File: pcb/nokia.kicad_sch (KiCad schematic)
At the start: 96 parts, among them J1 Conn_01x07, J2 USB_B_Micro, J20 Conn_01x04_Pin, J3 SM03B-SRSS-TB, J4 Conn_01x06_Pin, J5 Conn_02x10_Top_Bottom, J6 SM03B-SRSS-TB, M1 Vibration, Q1 BC847, SW1 SW_Push, U1 W25Q128JVS, U4 NCP1117-3.3_SOT223, U5 RP2350_80QFN, Y1 ABM8-272-T3

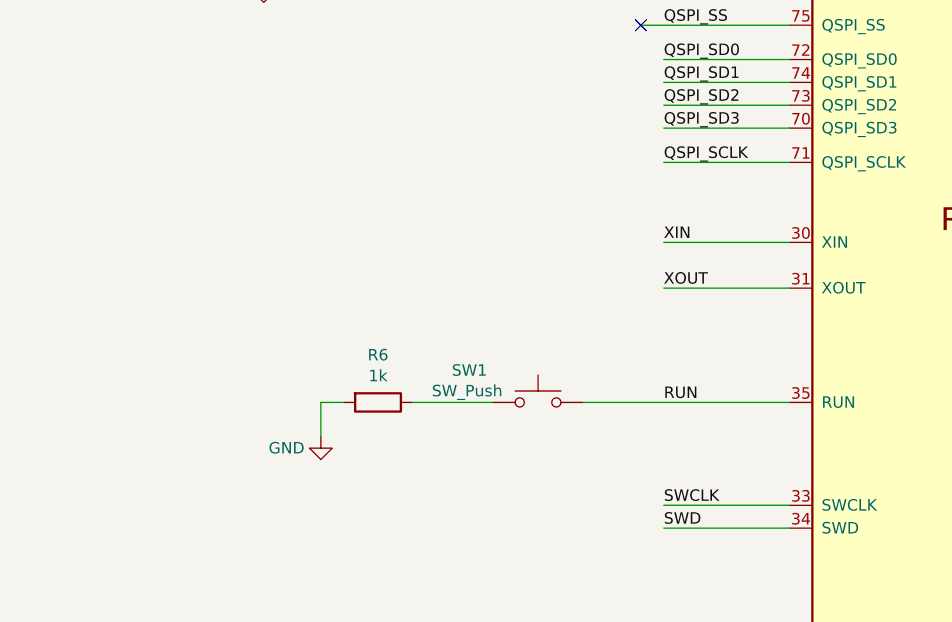
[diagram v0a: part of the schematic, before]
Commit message: power button can be gpio or run
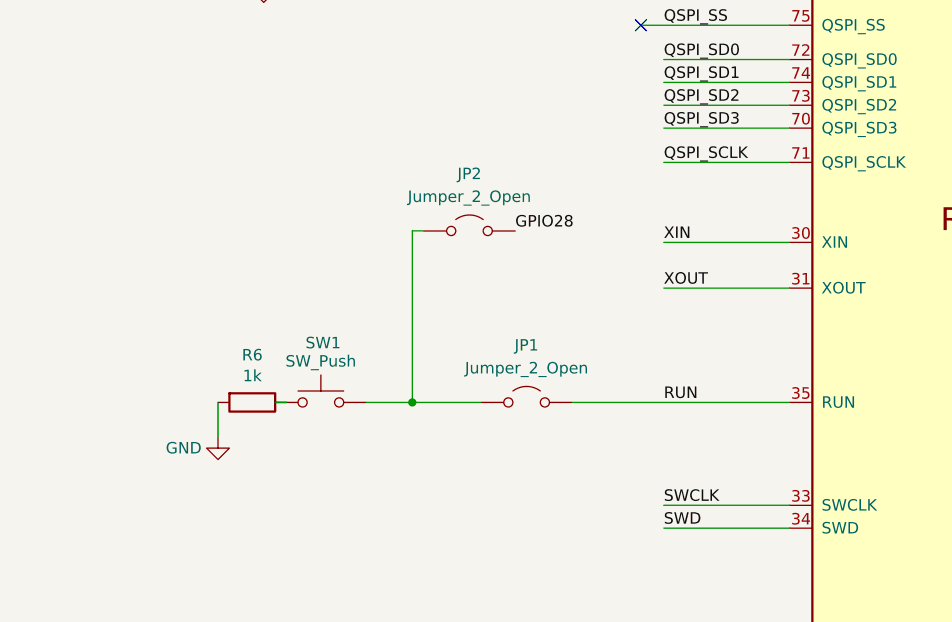
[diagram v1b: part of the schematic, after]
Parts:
- added JP1, JP2: Jumper_2_Open, Jumper:SolderJumper-2_P1.3mm_Open_RoundedPad1.0x1.5mm, symbol Jumper:Jumper_2_Open
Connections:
- net GPIO28: now also JP2.2 (B)
- net RUN: now also JP1.2 (B); no longer SW1.2
- new net: JP1.1 (A), JP2.1 (A), SW1.2
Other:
- moved on the sheet: R6, SW1
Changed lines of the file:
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@@
 	)
 	(junction
+		(at 200.66 129.54)
+		(diameter 0)
+		(color 0 0 0 0)
+	)
+	(junction
 		(at 373.38 36.83)
 		(diameter 0)
@@
 	(wire
 		(pts
+			(xy 200.66 129.54) (xy 208.28 129.54)
+		)
+		(stroke
+			(width 0)
+			(type default)
+		)
+	)
+	(wire
+		(pts
 			(xy 311.15 111.76) (xy 326.39 111.76)
 		)
@@
 	(wire
 		(pts
+			(xy 201.93 110.49) (xy 200.66 110.49)
+		)
+		(stroke
+			(width 0)
+			(type default)
+		)
+	)
+	(wire
+		(pts
 			(xy 90.17 212.09) (xy 90.17 208.28)
 		)
@@
 	(wire
 		(pts
+			(xy 218.44 129.54) (xy 242.57 129.54)
+		)
+		(stroke
+			(width 0)
+			(type default)
+		)
+	)
+	(wire
+		(pts
 			(xy 177.8 264.16) (xy 175.26 264.16)
 		)
@@
 	(wire
 		(pts
-			(xy 200.66 129.54) (xy 209.55 129.54)
+			(xy 186.69 129.54) (xy 185.42 129.54)
 		)
 		(stroke
@@
 	(wire
 		(pts
+			(xy 195.58 129.54) (xy 200.66 129.54)
+		)
+		(stroke
+			(width 0)
+			(type default)
+		)
+	)
+	(wire
+		(pts
 			(xy 127 259.08) (xy 127 257.81)
 		)
@@
 	(wire
 		(pts
-			(xy 219.71 129.54) (xy 242.57 129.54)
-		)
-		(stroke
-			(width 0)
-			(type default)
-		)
-	)
-	(wire
-		(pts
 			(xy 327.66 36.83) (xy 316.23 36.83)
 		)
@@
 	(wire
 		(pts
+			(xy 200.66 110.49) (xy 200.66 129.54)
+		)
+		(stroke
+			(width 0)
+			(type default)
+		)
+	)
+	(wire
+		(pts
 			(xy 264.16 45.72) (xy 270.51 45.72)
 		)
@@
 	(wire
 		(pts
-			(xy 190.5 129.54) (xy 190.5 133.35)
+			(xy 179.07 129.54) (xy 179.07 133.35)
 		)
 		(stroke
@@
 	(wire
 		(pts
-			(xy 193.04 129.54) (xy 190.5 129.54)
-		)
-		(stroke
-			(width 0)
-			(type default)
-		)
-	)
-	(wire
-		(pts
 			(xy 270.51 233.68) (xy 268.605 233.68)
 		)
@@
 		)
 	)
+	(label "GPIO28"
+		(at 212.09 110.49 0)
+		(fields_autoplaced yes)
+		(effects
+			(font
+				(size 1.27 1.27)
+			)
+			(justify left bottom)
+		)
+	)
 	(label "GPIO32"
 		(at 29.21 124.46 0)
@@
 	)
 	(symbol
+		(lib_id "Jumper:Jumper_2_Open")
+		(at 213.36 129.54 0)
+		(unit 1)
+		(exclude_from_sim yes)
+		(in_bom yes)
+		(on_board yes)
+		(dnp no)
+		(fields_autoplaced yes)
+		(property "Reference" "JP1"
+			(at 213.36 123.19 0)
+			(effects
+				(font
+					(size 1.27 1.27)
+				)
+			)
+		)
+		(property "Value" "Jumper_2_Open"
+			(at 213.36 125.73 0)
+			(effects
+				(font
+					(size 1.27 1.27)
+				)
+			)
+		)
+		(property "Footprint" "Jumper:SolderJumper-2_P1.3mm_Open_RoundedPad1.0x1.5mm"
+			(at 213.36 129.54 0)
+			(effects
+				(font
+					(size 1.27 1.27)
+				)
+				(hide yes)
+			)
+		)
+		(property "Datasheet" "~"
+			(at 213.36 129.54 0)
+			(effects
+				(font
+					(size 1.27 1.27)
+				)
+				(hide yes)
+			)
+		)
+		(property "Description" "Jumper, 2-pole, open"
+			(at 213.36 129.54 0)
+			(effects
+				(font
+					(size 1.27 1.27)
+				)
+				(hide yes)
+			)
+		)
+		(pin "1"
+		)
+		(pin "2"
+		)
+		(instances
+			(project ""
+				(path "/3906e17f-1a23-46f4-8c63-f34176cde9d9"
+					(reference "JP1")
+					(unit 1)
+				)
+			)
+		)
+	)
+	(symbol
 		(lib_name "LED_ARGB_1")
 		(lib_id "Device:LED_ARGB")
@@
 	(symbol
 		(lib_id "Device:R")
-		(at 196.85 129.54 270)
+		(at 182.88 129.54 270)
 		(unit 1)
 		(exclude_from_sim no)
@@
 		(dnp no)
 		(property "Reference" "R6"
-			(at 196.85 124.2822 90)
+			(at 182.88 124.2822 90)
 			(effects
 				(font
@@
 		)
 		(property "Value" "1k"
-			(at 196.85 126.5936 90)
+			(at 182.88 126.5936 90)
 			(effects
 				(font
@@
 		)
 		(property "Footprint" "Resistor_SMD:R_0402_1005Metric"
-			(at 196.85 127.762 90)
+			(at 182.88 127.762 90)
 			(effects
 				(font
@@
 		)
 		(property "Datasheet" "~"
-			(at 196.85 129.54 0)
+			(at 182.88 129.54 0)
 			(effects
 				(font
@@
 		)
 		(property "Description" ""
-			(at 196.85 129.54 0)
+			(at 182.88 129.54 0)
 			(effects
 				(font
@@
 	)
 	(symbol
+		(lib_id "Jumper:Jumper_2_Open")
+		(at 207.01 110.49 0)
+		(unit 1)
+		(exclude_from_sim yes)
+		(in_bom yes)
+		(on_board yes)
+		(dnp no)
+		(fields_autoplaced yes)
+		(property "Reference" "JP2"
+			(at 207.01 104.14 0)
+			(effects
+				(font
+					(size 1.27 1.27)
+				)
+			)
+		)
+		(property "Value" "Jumper_2_Open"
+			(at 207.01 106.68 0)
+			(effects
+				(font
+					(size 1.27 1.27)
+				)
+			)
+		)
+		(property "Footprint" "Jumper:SolderJumper-2_P1.3mm_Open_RoundedPad1.0x1.5mm"
+			(at 207.01 110.49 0)
+			(effects
+				(font
+					(size 1.27 1.27)
+				)
+				(hide yes)
+			)
+		)
+		(property "Datasheet" "~"
+			(at 207.01 110.49 0)
+			(effects
+				(font
+					(size 1.27 1.27)
+				)
+				(hide yes)
+			)
+		)
+		(property "Description" "Jumper, 2-pole, open"
+			(at 207.01 110.49 0)
+			(effects
+				(font
+					(size 1.27 1.27)
+				)
+				(hide yes)
+			)
+		)
+		(pin "1"
+		)
+		(pin "2"
+		)
+		(instances
+			(project "nokia"
+				(path "/3906e17f-1a23-46f4-8c63-f34176cde9d9"
+					(reference "JP2")
+					(unit 1)
+				)
+			)
+		)
+	)
+	(symbol
 		(lib_id "Device:R")
 		(at 64.77 116.84 180)
@@
 	(symbol
 		(lib_id "power:GND")
-		(at 190.5 133.35 0)
+		(at 179.07 133.35 0)
 		(unit 1)
 		(exclude_from_sim no)
@@
 		(dnp no)
 		(property "Reference" "#PWR024"
-			(at 190.5 139.7 0)
+			(at 179.07 139.7 0)
 			(effects
 				(font
@@
 		)
 		(property "Value" "GND"
-			(at 186.69 134.62 0)
+			(at 175.26 134.62 0)
 			(effects
 				(font
@@
 		)
 		(property "Footprint" ""
-			(at 190.5 133.35 0)
+			(at 179.07 133.35 0)
 			(effects
 				(font
@@
 		)
 		(property "Datasheet" ""
-			(at 190.5 133.35 0)
+			(at 179.07 133.35 0)
 			(effects
 				(font
@@
 		)
 		(property "Description" ""
-			(at 190.5 133.35 0)
+			(at 179.07 133.35 0)
 			(effects
 				(font
@@
 	(symbol
 		(lib_id "Switch:SW_Push")
-		(at 214.63 129.54 0)
+		(at 190.5 129.54 0)
 		(unit 1)
 		(exclude_from_sim no)
@@
 		(dnp no)
 		(property "Reference" "SW1"
-			(at 207.01 125.984 0)
+			(at 190.754 122.936 0)
 			(effects
 				(font
@@
 		)
 		(property "Value" "SW_Push"
-			(at 206.756 128.27 0)
+			(at 190.5 124.968 0)
 			(effects
 				(font
@@
 		)
 		(property "Footprint" "Button_Switch_SMD:power switch"
-			(at 214.63 124.46 0)
+			(at 190.5 124.46 0)
 			(effects
 				(font
@@
 		)
 		(property "Datasheet" "~"
-			(at 214.63 124.46 0)
+			(at 190.5 124.46 0)
 			(effects
 				(font
@@
 		)
 		(property "Description" "Push button switch, generic, two pins"
-			(at 214.63 129.54 0)
+			(at 190.5 129.54 0)
 			(effects
 				(font

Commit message: make corrections
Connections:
- net GPIO30: now also R11.1, R14.1, R16.1, R19.1, R22.1, R25.1, R28.1, R31.1; no longer R13.2, R18.2, R21.2, R24.2, R27.2, R30.2, R4.2, R5.2
- net GPIO32: now also R13.2, R18.2, R21.2, R24.2, R27.2, R30.2, R4.2, R5.2; no longer R11.1, R14.1, R16.1, R19.1, R22.1, R25.1, R28.1, R31.1
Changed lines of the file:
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@@
 		)
 	)
-	(label "GPIO32"
+	(label "GPIO30"
 		(at 52.07 210.82 0)
 		(fields_autoplaced yes)
@@
 		)
 	)
-	(label "GPIO30"
+	(label "GPIO32"
 		(at 46.99 213.36 0)
 		(fields_autoplaced yes)
@@
 		)
 	)
-	(label "GPIO30"
+	(label "GPIO32"
 		(at 93.98 175.26 0)
 		(fields_autoplaced yes)
@@
 		)
 	)
-	(label "GPIO30"
+	(label "GPIO32"
 		(at 52.07 127 0)
 		(fields_autoplaced yes)
@@
 		)
 	)
-	(label "GPIO30"
+	(label "GPIO32"
 		(at 90.17 212.09 0)
 		(fields_autoplaced yes)
@@
 		)
 	)
-	(label "GPIO30"
+	(label "GPIO32"
 		(at 46.99 172.72 0)
 		(fields_autoplaced yes)
@@
 		)
 	)
+	(label "GPIO32"
+		(at 106.68 127 0)
+		(fields_autoplaced yes)
+		(effects
+			(font
+				(size 1.27 1.27)
+			)
+			(justify left bottom)
+		)
+	)
 	(label "GPIO30"
-		(at 106.68 127 0)
-		(fields_autoplaced yes)
-		(effects
-			(font
-				(size 1.27 1.27)
-			)
-			(justify left bottom)
-		)
-	)
-	(label "GPIO32"
 		(at 95.25 209.55 0)
 		(fields_autoplaced yes)
@@
 		)
 	)
-	(label "GPIO32"
+	(label "GPIO30"
 		(at 85.09 124.46 0)
 		(fields_autoplaced yes)
@@
 		)
 	)
-	(label "GPIO32"
+	(label "GPIO30"
 		(at 29.21 124.46 0)
 		(fields_autoplaced yes)
@@
 		)
 	)
+	(label "GPIO30"
+		(at 52.07 170.18 0)
+		(fields_autoplaced yes)
+		(effects
+			(font
+				(size 1.27 1.27)
+			)
+			(justify left bottom)
+		)
+	)
 	(label "GPIO32"
-		(at 52.07 170.18 0)
-		(fields_autoplaced yes)
-		(effects
-			(font
-				(size 1.27 1.27)
-			)
-			(justify left bottom)
-		)
-	)
-	(label "GPIO30"
 		(at 24.13 127 0)
 		(fields_autoplaced yes)
@@
 		)
 	)
-	(label "GPIO32"
+	(label "GPIO30"
 		(at 111.76 124.46 0)
 		(fields_autoplaced yes)
@@
 		)
 	)
-	(label "GPIO32"
+	(label "GPIO30"
 		(at 99.06 172.72 0)
 		(fields_autoplaced yes)
@@
 		)
 	)
-	(label "GPIO32"
+	(label "GPIO30"
 		(at 57.15 124.46 0)
 		(fields_autoplaced yes)
@@
 		)
 	)
-	(label "GPIO30"
+	(label "GPIO32"
 		(at 80.01 127 0)
 		(fields_autoplaced yes)

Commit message: fix clearance for screws, more space for connectors, move LEDs
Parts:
- added C22, C24: 100n, Capacitor_SMD:C_0402_1005Metric, symbol Device:C
- added C23: 100m, 5V5, CoreElectronics_Components:Kemet_FC_10.5X5.5, symbol PiicoDev-Real-Time-Clock-RV3028-rescue:CP1-Device
- added JP4: I2C PU, CoreElectronics_Components:SolderJumper-3_P1.3mm_Closed_RoundedPad1.0x1.5mm_NumberLabels, symbol PiicoDev-Real-Time-Clock-RV3028-rescue:SolderJumper_3_Bridged123-Jumper
- added R34, R35, R36, R38: 10k, Resistor_SMD:R_0402_1005Metric, symbol Device:R
- added R37: 120R, Resistor_SMD:R_0402_1005Metric, symbol Device:R
- added R39: 100k, Resistor_SMD:R_0402_1005Metric, symbol Device:R
- added TP1: TestPoint, PiicoDev Real Time Clock RV3028:PinHeader_1x01_P2.54mm_Vertical, symbol Connector:TestPoint
- added Y2: RV-3028-C7_32.768kHz_1ppm_TA_QC, CoreElectronics_Components:MicroCrystal_RV3028C7, symbol CoreElectronics_Components:RV-3028-C7_32.768kHz_1ppm_TA_QC
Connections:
- net +3V3: now also C24.1, JP4.2 (C), R36.1, R38.1, R39.1, Y2.7 (VDD)
- net GND: now also C22.2, C23.2, C24.2, R39.2, Y2.5 (VSS)
- new net: JP4.1 (A), R35.1
- new net: JP4.3 (B), R34.1
- new net: C22.1, C23.1, TP1.1, Y2.6 (VBACKUP)
- new net: R37.1, Y2.4 (SDA)
- new net CLK: Y2.1 (CLKOUT)
- new net EVI: R38.2, Y2.8 (EVI)
- new net SCL: R34.2, Y2.3 (SCL)
- new net SDA: R35.2, R37.2
- new net ~{INT}: R36.2, Y2.2 (~{INT})
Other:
- note added: "Clear jumper to remove I2C pullup"
- note added: "I2C Pullups"
- moved on the sheet: D1, LS2, M1, Q1

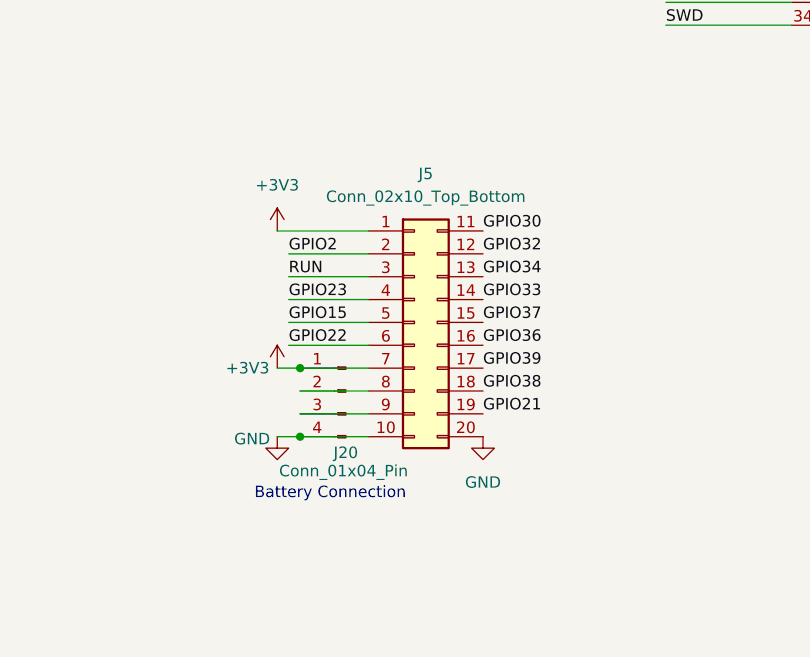
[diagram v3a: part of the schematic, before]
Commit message: remove prototyping connector
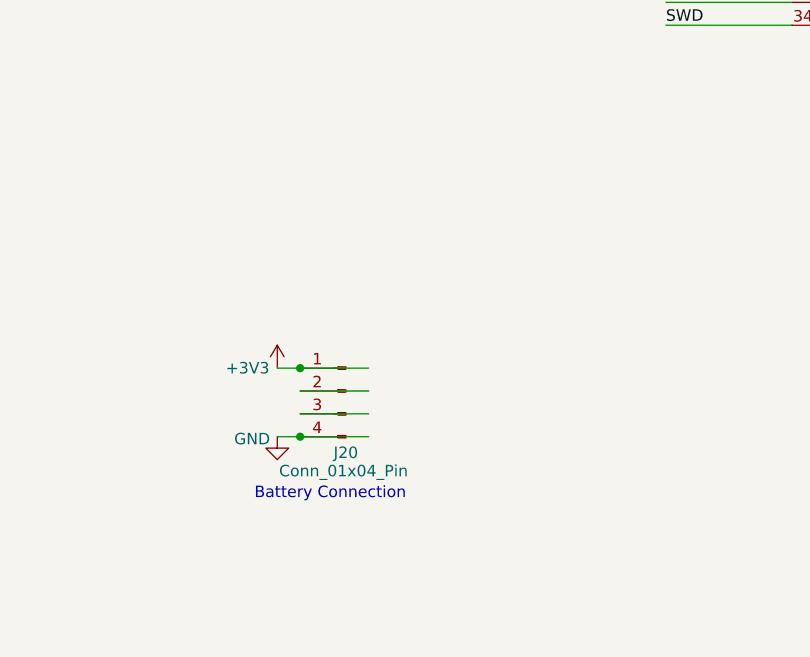
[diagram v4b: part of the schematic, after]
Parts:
- removed J5: Conn_02x10_Top_Bottom, Connector_PinHeader_2.54mm:PinHeader_2x10_P2.54mm_Vertical_SMD, symbol Connector_Generic:Conn_02x10_Top_Bottom

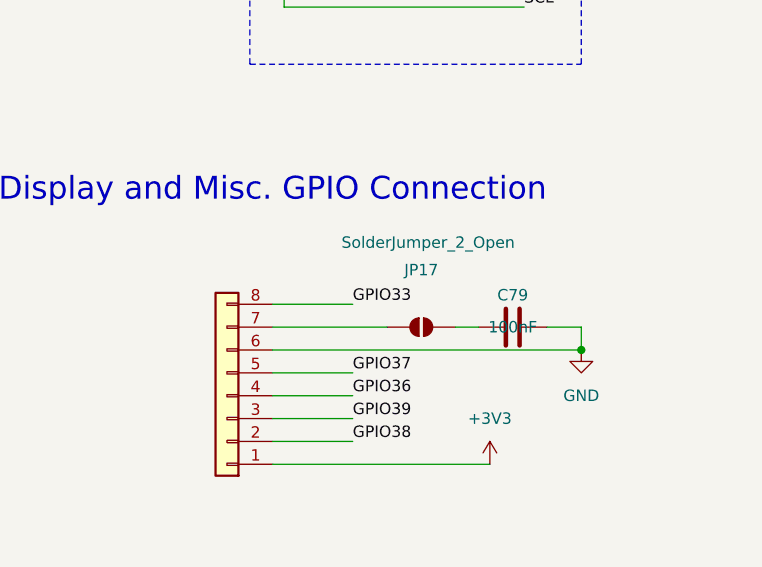
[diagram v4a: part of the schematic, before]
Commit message: remove display cap jumper
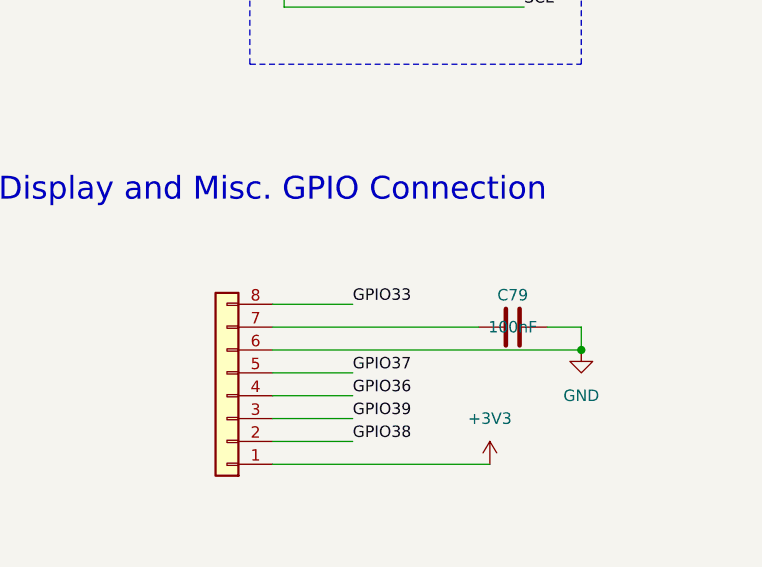
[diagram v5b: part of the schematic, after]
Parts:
- removed JP17: SolderJumper_2_Open, Jumper:SolderJumper-2_P1.3mm_Open_RoundedPad1.0x1.5mm, symbol Jumper:SolderJumper_2_Open
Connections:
- net at J1.7 (Pin_7): now also C79.2
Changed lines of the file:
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@@
 	(wire
 		(pts
-			(xy 365.76 229.87) (xy 378.46 229.87)
+			(xy 365.76 229.87) (xy 388.62 229.87)
 		)
 		(stroke
@@
 	(wire
 		(pts
-			(xy 386.08 229.87) (xy 388.62 229.87)
-		)
-		(stroke
-			(width 0)
-			(type default)
-		)
-	)
-	(wire
-		(pts
 			(xy 311.15 172.72) (xy 326.39 172.72)
 		)
@@
 					(unit 1)
 				)
-			)
-		)
-	)
-	(symbol
-		(lib_id "Jumper:SolderJumper_2_Open")
-		(at 382.27 229.87 0)
-		(unit 1)
-		(exclude_from_sim yes)
-		(in_bom no)
-		(on_board yes)
-		(dnp no)
-		(property "Reference" "JP17"
-			(at 382.27 223.52 0)
-			(effects
-				(font
-					(size 1.27 1.27)
-				)
-			)
-		)
-		(property "Value" "SolderJumper_2_Open"
-			(at 383.032 220.472 0)
-			(effects
-				(font
-					(size 1.27 1.27)
-				)
-			)
-		)
-		(property "Footprint" "Jumper:SolderJumper-2_P1.3mm_Open_RoundedPad1.0x1.5mm"
-			(at 382.27 229.87 0)
-			(effects
-				(font
-					(size 1.27 1.27)
-				)
-				(hide yes)
-			)
-		)
-		(property "Datasheet" "~"
-			(at 382.27 229.87 0)
-			(effects
-				(font
-					(size 1.27 1.27)
-				)
-				(hide yes)
-			)
-		)
-		(property "Description" "Solder Jumper, 2-pole, open"
-			(at 382.27 229.87 0)
-			(effects
-				(font
-					(size 1.27 1.27)
-				)
-				(hide yes)
-			)
-		)
-		(pin "1"
-		)
-		(pin "2"
-		)
-		(instances
-			(project ""
-				(path "/3906e17f-1a23-46f4-8c63-f34176cde9d9"
-					(reference "JP17")
-					(unit 1)
-				)

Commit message: add rtc and gauge, regulator
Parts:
- removed JP4: I2C PU, CoreElectronics_Components:SolderJumper-3_P1.3mm_Closed_RoundedPad1.0x1.5mm_NumberLabels, symbol PiicoDev-Real-Time-Clock-RV3028-rescue:SolderJumper_3_Bridged123-Jumper
- added C25: 1uF, symbol Device:C
- added R33, R40, R41: 10k, Resistor_SMD:R_0402_1005Metric, symbol Device:R
- added R42: 47k, Resistor_SMD:R_0402_1005Metric, symbol Device:R
- added R43: 100, Resistor_SMD:R_0402_1005Metric, symbol Device:R
- added U2: LC709203FQH-01TWG, Package_DFN_QFN:WDFN-8-1EP_4x3mm_P0.65mm_EP2.4x1.8mm, symbol Battery_Management:LC709203FQH-01TWG
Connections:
- net GPIO42_ADC2 is gone; now on net ~{INT}: U5.53 (GPIO42_ADC2)
- net GPIO46_ADC6 is gone; now on net SDA: U5.57 (GPIO46_ADC6)
- net GPIO47_ADC7 is gone; now on net SCL: U5.58 (GPIO47_ADC7)
- net +3V3: now also R34.1, R35.1, R33.1, R40.1, R41.1; no longer J20.1 (Pin_1)
- net GND: now also C25.2, U2.1 (TEST), U2.2 (V_{SS})
- net at J20.3 (Pin_3): now also R42.1, R43.1
- net GPIO43_ADC3 renamed ALARMB
- net ALARMB: now also R41.2, U2.4 (~{ALARMB})
- net GPIO44_ADC4 renamed SDA0
- net SDA0: now also R40.2, U2.7 (SDA)
- net GPIO45_ADC5 renamed SCL0
- net SCL0: now also R33.2, U2.8 (SCL)
- new net: R43.2, U2.6 (T_{SENSE})
- new net: C25.1, J20.1 (Pin_1), U2.3 (V_{DD})
- new net: R42.2, U2.5 (T_{SW})
- no-connect marks 3 -> 6
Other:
- note added: "I2C0 Pullups"
- moved on the sheet: C24, C79, J20, R34, R35, R39

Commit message: pcb v0.2
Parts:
- removed C25: 1uF, symbol Device:C
- removed J4: Conn_01x06_Pin, Connector:sim connector connector, symbol Connector:SIM_Card
- removed JP1, JP2: Jumper_2_Open, Jumper:SolderJumper-2_P1.3mm_Open_RoundedPad1.0x1.5mm, symbol Jumper:Jumper_2_Open
- removed R33, R40, R41: 10k, Resistor_SMD:R_0402_1005Metric, symbol Device:R
- removed R42: 47k, Resistor_SMD:R_0402_1005Metric, symbol Device:R
- removed R43: 100, Resistor_SMD:R_0402_1005Metric, symbol Device:R
- removed U2: LC709203FQH-01TWG, Package_DFN_QFN:WDFN-8-1EP_4x3mm_P0.65mm_EP2.4x1.8mm, symbol Battery_Management:LC709203FQH-01TWG
- added J5, J7: Conn_01x03_Pin, Connector_PinHeader_2.54mm:PinHeader_1x03_P2.54mm_Vertical, symbol Connector:Conn_01x03_Pin
- added R44, R45, R46, R47, R48, R49, R50, R51, R52, R53, R54, R55, R56, R57, R58, R59: 3k, Resistor_SMD:R_0402_1005Metric, symbol Device:R
- R6: value 1k -> 3k
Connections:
- net +3V3: now also J20.1 (Pin_1), R6.1, R44.2, R45.2, R46.2, R47.2, R48.2, R49.2, R50.1, R51.1, R52.1, R53.2, R54.2, R55.2, R56.2, R57.1, R58.1, R59.1; no longer KP#1.1 (A), KP*1.1 (A), KP0.1 (A), KP1.1 (A), KP2.1 (A), KP3.1 (A), KP4.1 (A), KP5.1 (A), KP6.1 (A), KP7.1 (A), KP8.1 (A), KP9.1 (A), KPC1.1 (A), KPDOWN1.1 (A), KPSELECT1.1 (A), KPUP1.1 (A)
- net GND: now also KP#1.1 (A), KP*1.1 (A), KP0.1 (A), KP1.1 (A), KP2.1 (A), KP3.1 (A), KP4.1 (A), KP5.1 (A), KP6.1 (A), KP7.1 (A), KP8.1 (A), KP9.1 (A), KPC1.1 (A), KPDOWN1.1 (A), KPSELECT1.1 (A), KPUP1.1 (A), SW1.1, J5.2 (Pin_2), J7.2 (Pin_2); no longer R6.2
- net GPIO0: now also J7.3 (Pin_3)
- net GPIO1: now also J7.1 (Pin_1)
- net GPIO10: now also R45.1
- net GPIO11: now also R48.1
- net GPIO12: now also R56.1
- net GPIO13: now also R54.1
- net GPIO14: now also R51.2
- net GPIO16: now also R59.2
- net GPIO17: now also R53.1
- net GPIO18: now also R50.2
- net GPIO19: now also R49.1
- net GPIO20: now also R44.1
- net GPIO28: now also R6.2, SW1.2
- net GPIO4: now also R46.1
- net GPIO5: now also R47.1
- net GPIO6: now also R52.2
- net GPIO7: now also R55.1
- net GPIO8: now also R58.2
- net GPIO9: now also R57.2
- net RUN: no longer U5.35 (RUN)
- net SWCLK: now also J5.1 (Pin_1)
- net SWD: now also J5.3 (Pin_3)
- no-connect marks 6 -> 4
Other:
- note removed: "I2C0 Pullups"
- note removed: "SIM Card Tray Connector"
